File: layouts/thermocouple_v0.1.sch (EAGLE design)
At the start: 28 parts, among them J1 1X2-3.5MM, J2 1X2-3.5MM, J3 1X2-3.5MM, J4 1X2-3.5MM, U1 MAX31855, U2 MAX31855, U3 MAX31855, U4 MAX31855, U5 MAX8687

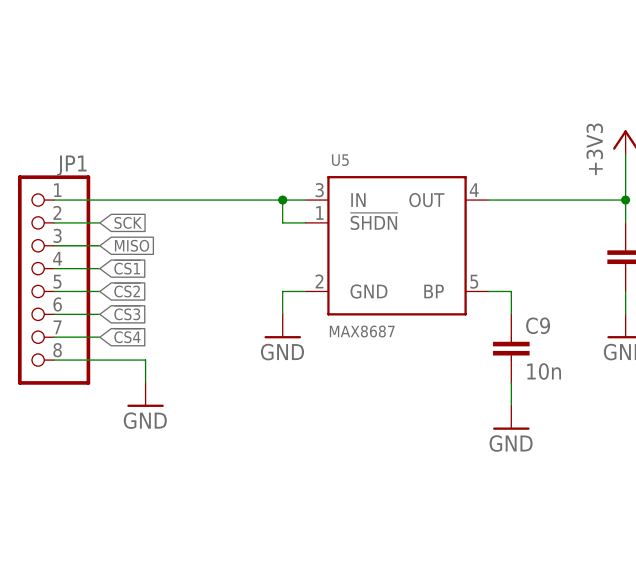
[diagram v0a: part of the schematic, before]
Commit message: fixed eagle errors due to upgrade to 6.5
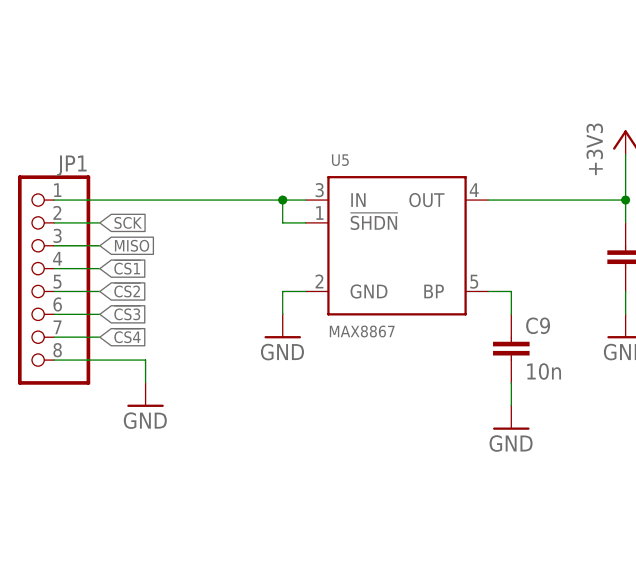
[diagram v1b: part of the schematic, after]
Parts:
- U5: value MAX8687 -> MAX8867; device maxim:MAX8687 -> maxim:MAX8867
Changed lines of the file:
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@@
 <?xml version="1.0" encoding="utf-8"?>
 <!DOCTYPE eagle SYSTEM "eagle.dtd">
-<eagle version="6.3">
+<eagle version="6.6.0">
 <drawing>
 <settings>
@@
 <part name="FRAME1" library="frames" deviceset="A4L-LOC" device=""/>
 <part name="U1" library="maxim" deviceset="MAX31855" device=""/>
-<part name="U5" library="maxim" deviceset="MAX8687" device=""/>
+<part name="U5" library="maxim" deviceset="MAX8867" device=""/>
 <part name="+3V1" library="supply1" deviceset="+3V3" device=""/>
 <part name="C1" library="rcl" deviceset="C-EU" device="C0603" value="100n"/>
@@
 <wire x1="134.62" y1="147.32" x2="132.08" y2="147.32" width="0.1524" layer="91"/>
 <label x="132.08" y="147.32" size="1.27" layer="95" rot="R180" xref="yes"/>
-<wire x1="30.48" y1="104.14" x2="25.4" y2="104.14" width="0.1524" layer="91"/>
-<pinref part="JP1" gate="A" pin="3"/>
-<label x="30.48" y="104.14" size="1.27" layer="95" xref="yes"/>
 </segment>
 <segment>
@@
 <label x="132.08" y="53.34" size="1.27" layer="95" rot="R180" xref="yes"/>
 </segment>
+<segment>
+<pinref part="JP1" gate="A" pin="3"/>
+<wire x1="25.4" y1="104.14" x2="30.48" y2="104.14" width="0.1524" layer="91"/>
+<label x="30.48" y="104.14" size="1.27" layer="95" xref="yes"/>
+</segment>
 </net>
 <net name="SCK" class="0">
@@
 <wire x1="134.62" y1="144.78" x2="132.08" y2="144.78" width="0.1524" layer="91"/>
 <label x="132.08" y="144.78" size="1.27" layer="95" rot="R180" xref="yes"/>
-<wire x1="30.48" y1="106.68" x2="25.4" y2="106.68" width="0.1524" layer="91"/>
-<pinref part="JP1" gate="A" pin="2"/>
-<label x="30.48" y="106.68" size="1.27" layer="95" xref="yes"/>
 </segment>
 <segment>
@@
 <label x="132.08" y="50.8" size="1.27" layer="95" rot="R180" xref="yes"/>
 </segment>
+<segment>
+<pinref part="JP1" gate="A" pin="2"/>
+<wire x1="25.4" y1="106.68" x2="30.48" y2="106.68" width="0.1524" layer="91"/>
+<label x="30.48" y="106.68" size="1.27" layer="95" xref="yes"/>
+</segment>
 </net>
 <net name="!CS1" class="0">
@@
 <wire x1="134.62" y1="142.24" x2="132.08" y2="142.24" width="0.1524" layer="91"/>
 <label x="132.08" y="142.24" size="1.27" layer="95" rot="R180" xref="yes"/>
-<wire x1="30.48" y1="101.6" x2="25.4" y2="101.6" width="0.1524" layer="91"/>
+</segment>
+<segment>
 <pinref part="JP1" gate="A" pin="4"/>
+<wire x1="25.4" y1="101.6" x2="30.48" y2="101.6" width="0.1524" layer="91"/>
 <label x="30.48" y="101.6" size="1.27" layer="95" xref="yes"/>
 </segment>
@@
 <wire x1="134.62" y1="48.26" x2="132.08" y2="48.26" width="0.1524" layer="91"/>
 <label x="132.08" y="48.26" size="1.27" layer="95" rot="R180" xref="yes"/>
-<wire x1="30.48" y1="93.98" x2="25.4" y2="93.98" width="0.1524" layer="91"/>
+</segment>
+<segment>
 <pinref part="JP1" gate="A" pin="7"/>
+<wire x1="25.4" y1="93.98" x2="30.48" y2="93.98" width="0.1524" layer="91"/>
 <label x="30.48" y="93.98" size="1.27" layer="95" xref="yes"/>
 </segment>
@@
 <wire x1="134.62" y1="78.74" x2="132.08" y2="78.74" width="0.1524" layer="91"/>
 <label x="132.08" y="78.74" size="1.27" layer="95" rot="R180" xref="yes"/>
-<wire x1="30.48" y1="96.52" x2="25.4" y2="96.52" width="0.1524" layer="91"/>
+</segment>
+<segment>
 <pinref part="JP1" gate="A" pin="6"/>
+<wire x1="25.4" y1="96.52" x2="30.48" y2="96.52" width="0.1524" layer="91"/>
 <label x="30.48" y="96.52" size="1.27" layer="95" xref="yes"/>
 </segment>
@@
 <wire x1="134.62" y1="109.22" x2="132.08" y2="109.22" width="0.1524" layer="91"/>
 <label x="132.08" y="109.22" size="1.27" layer="95" rot="R180" xref="yes"/>
-<wire x1="30.48" y1="99.06" x2="25.4" y2="99.06" width="0.1524" layer="91"/>
+</segment>
+<segment>
 <pinref part="JP1" gate="A" pin="5"/>
+<wire x1="25.4" y1="99.06" x2="30.48" y2="99.06" width="0.1524" layer="91"/>
 <label x="30.48" y="99.06" size="1.27" layer="95" xref="yes"/>
 </segment>
@@
 </sheet>
 </sheets>
+<errors>
+</errors>
 </schematic>
 </drawing>
